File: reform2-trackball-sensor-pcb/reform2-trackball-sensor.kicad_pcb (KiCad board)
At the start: 2 copper layers, 23.8 x 17.8 mm, 14 parts, among them J1 Conn_01x06_Male, U1 PAT9125EL

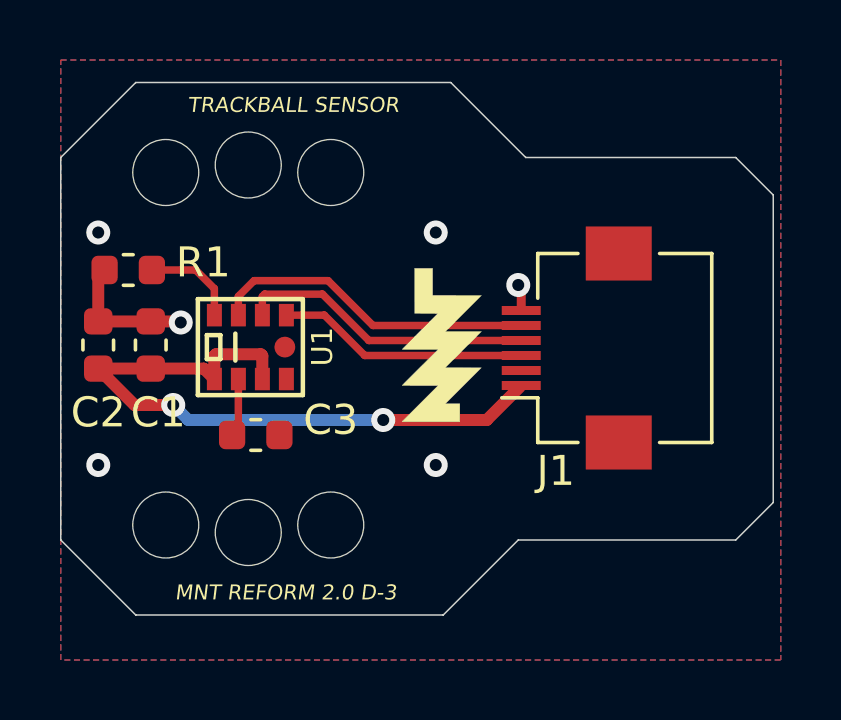
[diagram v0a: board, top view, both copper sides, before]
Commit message: WIP trackball sensor now CERN-OHL-S 2.0
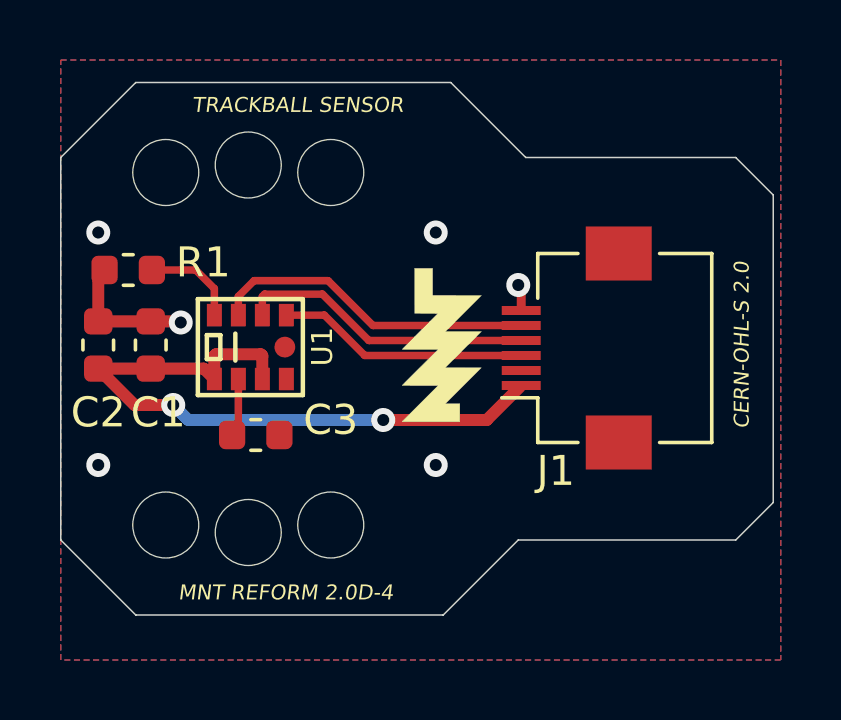
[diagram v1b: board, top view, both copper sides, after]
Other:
- board text added: "CERN-OHL-S 2.0"
- board text added: "MNT REFORM 2.0D-4"
- board text removed: "MNT REFORM 2.0 D-3"
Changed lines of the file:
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@@
-(kicad_pcb (version 20171130) (host pcbnew 5.1.2+dfsg1-1)
+(kicad_pcb (version 20171130) (host pcbnew 5.1.5+dfsg1-2+b1)
   (general
     (thickness 1)
-    (drawings 16)
+    (drawings 17)
     (tracks 49)
     (zones 0)
@@
     )
   )
+  (gr_text "CERN-OHL-S 2.0" (at 166.2 81.5 90) (layer F.SilkS)
+    (effects (font (size 0.5 0.5) (thickness 0.1) italic))
+  )
   (gr_line (start 156.25 90.5) (end 158.75 88) (layer Edge.Cuts) (width 0.05))
   (gr_line (start 156.5 72.75) (end 159 75.25) (layer Edge.Cuts) (width 0.05))
   (gr_circle (center 149.7 87.8) (end 158.75 96.25) (layer Dwgs.User) (width 0.15))
   (gr_circle (center 149.75 75.5) (end 160.5 81.5) (layer Dwgs.User) (width 0.15))
-  (gr_text "MNT REFORM 2.0 D-3" (at 151 89.75) (layer F.SilkS)
+  (gr_text "MNT REFORM 2.0D-4" (at 151 89.75) (layer F.SilkS)
     (effects (font (size 0.5 0.5) (thickness 0.1) italic))
   )
@@
   (gr_line (start 146 72.75) (end 143.5 75.25) (layer Edge.Cuts) (width 0.05))
   (gr_line (start 167.25 76.5) (end 167.25 86.75) (layer Edge.Cuts) (width 0.05))
-  (gr_text "TRACKBALL SENSOR " (at 151.25 73.5) (layer F.SilkS)
+  (gr_text "TRACKBALL SENSOR " (at 151.4 73.5) (layer F.SilkS)
     (effects (font (size 0.5 0.5) (thickness 0.1) italic))
   )

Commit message: WIP: reform2-trackball-sensor: remove superfluous holes
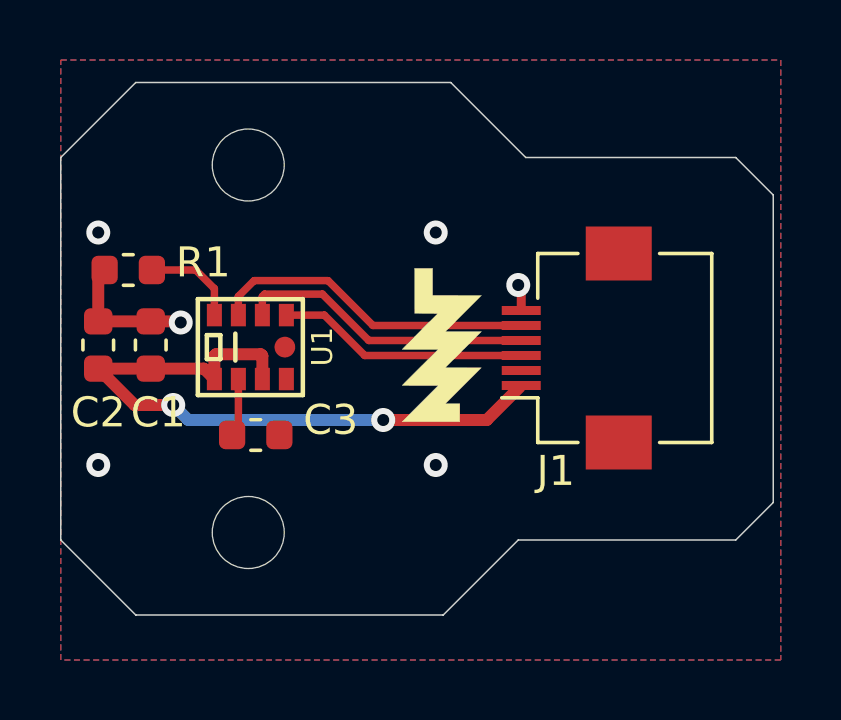
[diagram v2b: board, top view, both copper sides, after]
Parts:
- removed H1, H3, H4, H6: MountingHole, MountingHole:MountingHole_2.2mm_M2
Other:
- board text removed: "CERN-OHL-S 2.0"
- board text removed: "MNT REFORM 2.0D-4"
- board text removed: "TRACKBALL SENSOR"
